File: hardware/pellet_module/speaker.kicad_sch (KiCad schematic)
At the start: 8 parts, among them U3 TPA2005D1

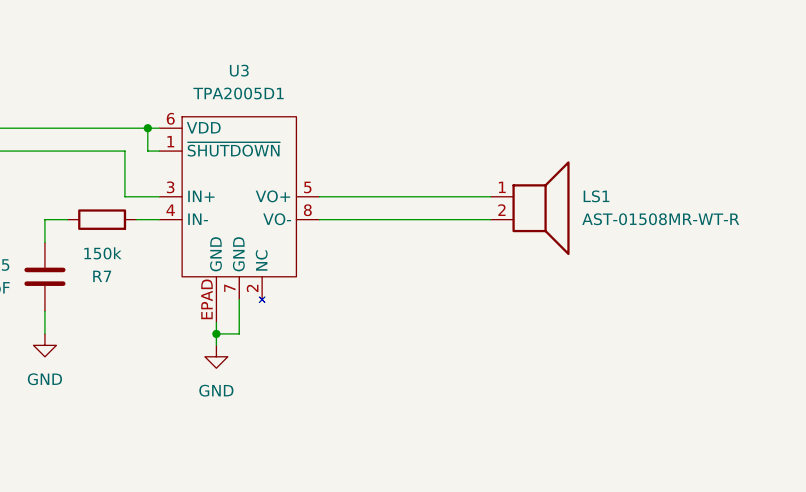
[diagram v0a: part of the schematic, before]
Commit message: add test points, mpns, datasheets
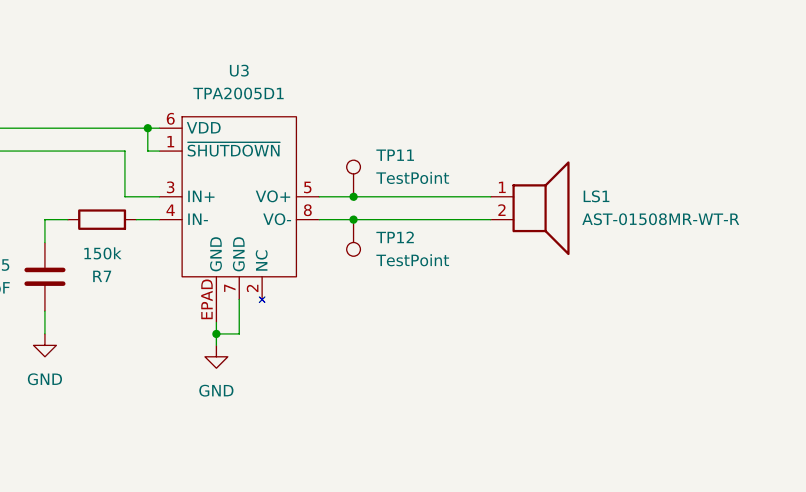
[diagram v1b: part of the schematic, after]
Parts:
- added TP11, TP12: TestPoint, symbol Connector:TestPoint
- C13: footprint (none) -> Capacitor_SMD:C_0603_1608Metric; MPN (none) -> CC0603KRX7R7BB105
- C14, C15: footprint (none) -> Capacitor_SMD:C_0603_1608Metric; MPN (none) -> GRM1885C1H510JA01D
- LS1: MPN (none) -> AST-01508MR-WT-R
- R6: MPN (none) -> RC0603FR-0715KL
- R7: MPN (none) -> RC0603FR-07150KL
- U3: footprint (none) -> Package_SO:HVSSOP-8-1EP_3x3mm_P0.65mm_EP1.57x1.89mm; MPN (none) -> TPA2005D1DRBR
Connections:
- net at LS1.1, U3.5 (VO+): now also TP11.1
- net at LS1.2, U3.8 (VO-): now also TP12.1
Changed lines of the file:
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@@
 	(paper "A4")
+	(junction
+		(at 222.25 96.52)
+		(diameter 0)
+		(color 0 0 0 0)
+	)
 	(junction
 		(at 207.01 111.76)
@@
 		(color 0 0 0 0)
 	)
+	(junction
+		(at 222.25 99.06)
+		(diameter 0)
+		(color 0 0 0 0)
+	)
 	(no_connect
 		(at 173.99 96.52)
@@
 	(wire
 		(pts
+			(xy 222.25 96.52) (xy 237.49 96.52)
+		)
+		(stroke
+			(width 0)
+			(type default)
+		)
+	)
+	(wire
+		(pts
 			(xy 209.55 107.95) (xy 209.55 111.76)
 		)
@@
 	(wire
 		(pts
-			(xy 218.44 96.52) (xy 237.49 96.52)
+			(xy 218.44 96.52) (xy 222.25 96.52)
 		)
 		(stroke
@@
 	(wire
 		(pts
+			(xy 222.25 99.06) (xy 237.49 99.06)
+		)
+		(stroke
+			(width 0)
+			(type default)
+		)
+	)
+	(wire
+		(pts
 			(xy 207.01 110.49) (xy 207.01 111.76)
 		)
@@
 	(wire
 		(pts
-			(xy 218.44 99.06) (xy 237.49 99.06)
+			(xy 218.44 99.06) (xy 222.25 99.06)
 		)
 		(stroke
@@
 			)
 		)
-		(property "MPN" ""
+		(property "MPN" "RC0603FR-0715KL"
 			(at 160.02 96.52 0)
 			(effects
@@
 			)
 		)
-		(property "MPN" ""
+		(property "MPN" "AST-01508MR-WT-R"
 			(at 242.57 96.52 0)
 			(effects
@@
 			)
 		)
-		(property "MPN" ""
+		(property "MPN" "RC0603FR-07150KL"
 			(at 194.31 99.06 0)
 			(effects
@@
 				(path "/48650363-a452-429d-997e-1ddabb69aad0/b6dbd572-5e20-467e-a878-ec4193e43632"
 					(reference "R7")
+					(unit 1)
+				)
+			)
+		)
+	)
+	(symbol
+		(lib_id "Connector:TestPoint")
+		(at 222.25 96.52 0)
+		(unit 1)
+		(exclude_from_sim no)
+		(in_bom yes)
+		(on_board yes)
+		(dnp no)
+		(fields_autoplaced yes)
+		(property "Reference" "TP11"
+			(at 224.79 91.9479 0)
+			(effects
+				(font
+					(size 1.27 1.27)
+				)
+				(justify left)
+			)
+		)
+		(property "Value" "TestPoint"
+			(at 224.79 94.4879 0)
+			(effects
+				(font
+					(size 1.27 1.27)
+				)
+				(justify left)
+			)
+		)
+		(property "Footprint" ""
+			(at 227.33 96.52 0)
+			(effects
+				(font
+					(size 1.27 1.27)
+				)
+				(hide yes)
+			)
+		)
+		(property "Datasheet" "~"
+			(at 227.33 96.52 0)
+			(effects
+				(font
+					(size 1.27 1.27)
+				)
+				(hide yes)
+			)
+		)
+		(property "Description" "test point"
+			(at 222.25 96.52 0)
+			(effects
+				(font
+					(size 1.27 1.27)
+				)
+				(hide yes)
+			)
+		)
+		(pin "1"
+		)
+		(instances
+			(project ""
+				(path "/48650363-a452-429d-997e-1ddabb69aad0/b6dbd572-5e20-467e-a878-ec4193e43632"
+					(reference "TP11")
+					(unit 1)
+				)
+			)
+		)
+	)
+	(symbol
+		(lib_id "Connector:TestPoint")
+		(at 222.25 99.06 180)
+		(unit 1)
+		(exclude_from_sim no)
+		(in_bom yes)
+		(on_board yes)
+		(dnp no)
+		(fields_autoplaced yes)
+		(property "Reference" "TP12"
+			(at 224.79 101.0919 0)
+			(effects
+				(font
+					(size 1.27 1.27)
+				)
+				(justify right)
+			)
+		)
+		(property "Value" "TestPoint"
+			(at 224.79 103.6319 0)
+			(effects
+				(font
+					(size 1.27 1.27)
+				)
+				(justify right)
+			)
+		)
+		(property "Footprint" ""
+			(at 217.17 99.06 0)
+			(effects
+				(font
+					(size 1.27 1.27)
+				)
+				(hide yes)
+			)
+		)
+		(property "Datasheet" "~"
+			(at 217.17 99.06 0)
+			(effects
+				(font
+					(size 1.27 1.27)
+				)
+				(hide yes)
+			)
+		)
+		(property "Description" "test point"
+			(at 222.25 99.06 0)
+			(effects
+				(font
+					(size 1.27 1.27)
+				)
+				(hide yes)
+			)
+		)
+		(pin "1"
+		)
+		(instances
+			(project "pellet"
+				(path "/48650363-a452-429d-997e-1ddabb69aad0/b6dbd572-5e20-467e-a878-ec4193e43632"
+					(reference "TP12")
 					(unit 1)
 				)
@@
 			)
 		)
-		(property "Footprint" ""
+		(property "Footprint" "Package_SO:HVSSOP-8-1EP_3x3mm_P0.65mm_EP1.57x1.89mm"
 			(at 209.55 85.09 0)
 			(effects
@@
 			)
 		)
-		(property "Datasheet" ""
+		(property "Datasheet" "https://www.ti.com/lit/ds/symlink/tpa2005d1.pdf"
 			(at 209.55 85.09 0)
 			(effects
@@
 			)
 		)
-		(property "MPN" ""
+		(property "MPN" "TPA2005D1DRBR"
 			(at 209.55 85.09 0)
 			(effects
@@
 			)
 		)
-		(property "Footprint" ""
+		(property "Footprint" "Capacitor_SMD:C_0603_1608Metric"
 			(at 188.9252 109.22 0)
 			(effects
@@
 			)
 		)
-		(property "MPN" ""
+		(property "MPN" "GRM1885C1H510JA01D"
 			(at 187.96 105.41 0)
 			(effects
@@
 			)
 		)
-		(property "Footprint" ""
+		(property "Footprint" "Capacitor_SMD:C_0603_1608Metric"
 			(at 120.3452 102.87 0)
 			(effects
@@
 			)
 		)
-		(property "MPN" ""
+		(property "MPN" "CC0603KRX7R7BB105"
 			(at 119.38 99.06 0)
 			(effects
@@
 			)
 		)
-		(property "Footprint" ""
+		(property "Footprint" "Capacitor_SMD:C_0603_1608Metric"
 			(at 151.13 97.4852 0)
 			(effects
@@
 			)
 		)
-		(property "MPN" ""
+		(property "MPN" "GRM1885C1H510JA01D"
 			(at 147.32 96.52 0)
 			(effects

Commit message: add titles, ESD protection, make changes requested by Ryan
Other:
- company: (none) -> Christie Lab, CU-Anschutz
- title: (none) -> Autotrainer Pellet Module - Speaker
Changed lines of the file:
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@@
 	(generator_version "8.0")
 	(paper "A4")
+	(title_block
+		(title "Autotrainer Pellet Module - Speaker")
+		(date "2024-07-09")
+		(rev "v1.0")
+		(company "Christie Lab, CU-Anschutz")
+		(comment 1 "Prepared by LeafLabs, LLC")
+	)
 	(junction
 		(at 222.25 96.52)

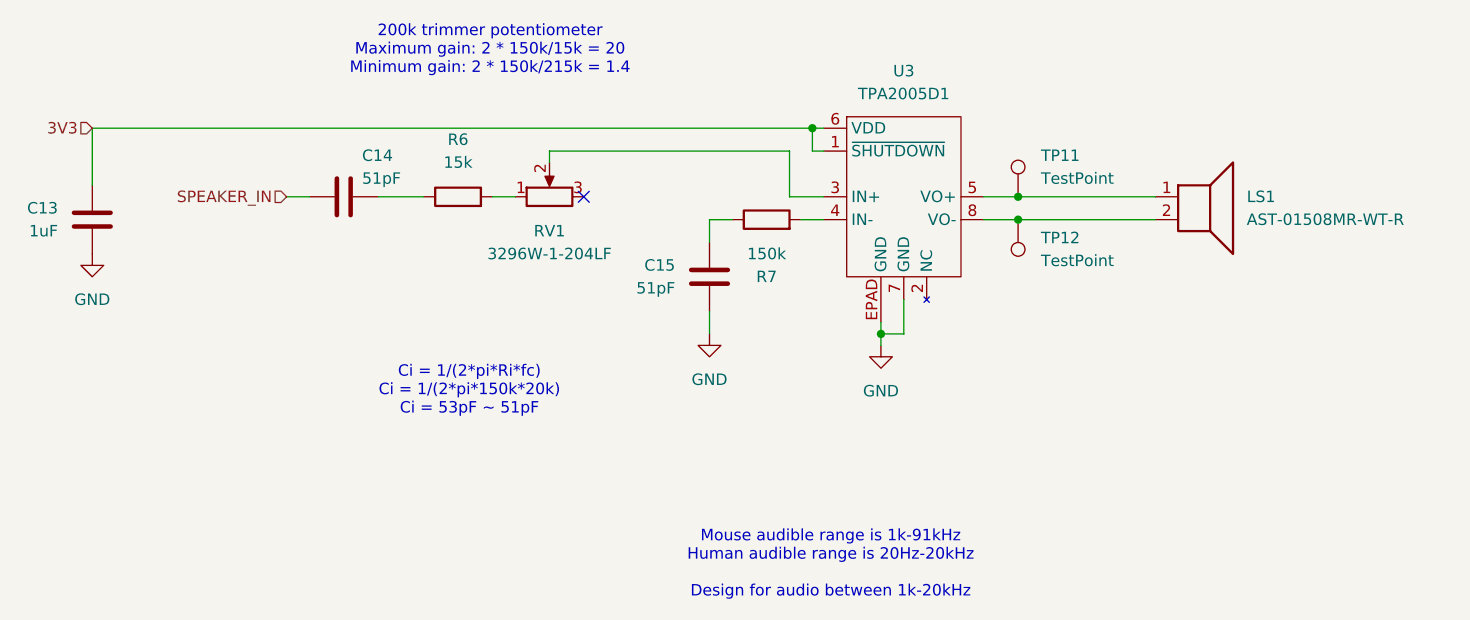
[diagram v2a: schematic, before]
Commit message: * Add footprints for every part * Change power LED from 20mA to 4mA * Edit symbols to match footprints (EPAD -> pin numbers) to eliminate errors on import to pcbnew
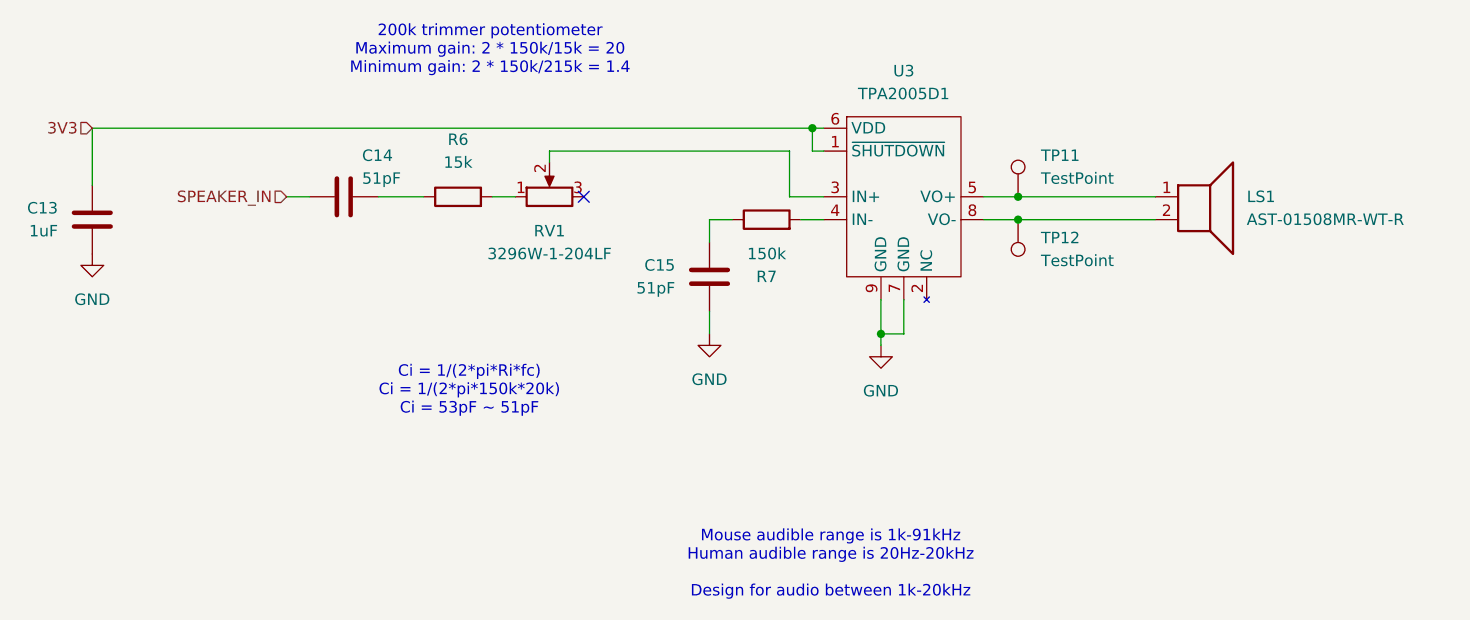
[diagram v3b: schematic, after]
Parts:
- LS1: footprint (none) -> Leaf_Microphone:Speaker_P7.6mm
- R6, R7: footprint (none) -> Resistor_SMD:R_0603_1608Metric
- RV1: footprint (none) -> Potentiometer_THT:Potentiometer_Bourns_3296W_Vertical
- TP11, TP12: footprint (none) -> TestPoint:TestPoint_Pad_1.0x1.0mm
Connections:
- net GND: now also U3.9 (GND); no longer U3.EPAD (GND)
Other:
- moved on the sheet: U3
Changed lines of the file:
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@@
 	(wire
 		(pts
-			(xy 207.01 110.49) (xy 207.01 111.76)
+			(xy 207.01 107.95) (xy 207.01 111.76)
 		)
 		(stroke
@@
 			)
 		)
-		(property "Footprint" ""
+		(property "Footprint" "Resistor_SMD:R_0603_1608Metric"
 			(at 160.02 98.298 90)
 			(effects
@@
 			)
 		)
-		(property "Footprint" ""
+		(property "Footprint" "Potentiometer_THT:Potentiometer_Bourns_3296W_Vertical"
 			(at 170.18 96.52 0)
 			(effects
@@
 			)
 		)
-		(property "Footprint" ""
+		(property "Footprint" "Leaf_Microphone:Speaker_P7.6mm"
 			(at 242.57 101.6 0)
 			(effects
@@
 			)
 		)
-		(property "Footprint" ""
+		(property "Footprint" "Resistor_SMD:R_0603_1608Metric"
 			(at 194.31 100.838 90)
 			(effects
@@
 			)
 		)
-		(property "Footprint" ""
+		(property "Footprint" "TestPoint:TestPoint_Pad_1.0x1.0mm"
 			(at 227.33 96.52 0)
 			(effects
@@
 			)
 		)
-		(property "Footprint" ""
+		(property "Footprint" "TestPoint:TestPoint_Pad_1.0x1.0mm"
 			(at 217.17 99.06 0)
 			(effects
@@
 		(pin "5"
 		)
-		(pin "EPAD"
+		(pin "9"
 		)
 		(pin "3"

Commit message: Releases layout for pellet, magnet, and Jetson breakout boards.
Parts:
- C13: LCSC (none) -> C15849; MPN CC0603KRX7R7BB105 -> CL10A105KB8NNNC
- C14, C15: LCSC (none) -> C162235
- LS1: LCSC (none) -> C3311279
- R6: LCSC (none) -> C22809; MPN RC0603FR-0715KL -> 0603WAF1502T5E
- R7: LCSC (none) -> C22807; MPN RC0603FR-07150KL -> 0603WAF1503T5E
- RV1: LCSC (none) -> C58354
- TP11, TP12: now left out of the parts list
- U3: footprint Package_SO:HVSSOP-8-1EP_3x3mm_P0.65mm_EP1.57x1.89mm -> Leaf_InterfaceIC:HVSSOP-8-1EP_3x3mm_P0.65mm_EP1.57x1.89mm_SmallPads; LCSC (none) -> C27396; MPN TPA2005D1DRBR -> TPA2005D1DGNR
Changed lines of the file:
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@@
 			)
 		)
-		(property "MPN" "RC0603FR-0715KL"
+		(property "MPN" "0603WAF1502T5E"
+			(at 160.02 96.52 0)
+			(effects
+				(font
+					(size 1.27 1.27)
+				)
+				(hide yes)
+			)
+		)
+		(property "LCSC" "C22809"
 			(at 160.02 96.52 0)
 			(effects
@@
 			)
 		)
+		(property "LCSC" "C58354"
+			(at 170.18 96.52 0)
+			(effects
+				(font
+					(size 1.27 1.27)
+				)
+				(hide yes)
+			)
+		)
 		(pin "3"
 		)
@@
 			)
 		)
+		(property "LCSC" "C3311279"
+			(at 242.57 96.52 0)
+			(effects
+				(font
+					(size 1.27 1.27)
+				)
+				(hide yes)
+			)
+		)
 		(pin "2"
 		)
@@
 			)
 		)
-		(property "MPN" "RC0603FR-07150KL"
+		(property "MPN" "0603WAF1503T5E"
+			(at 194.31 99.06 0)
+			(effects
+				(font
+					(size 1.27 1.27)
+				)
+				(hide yes)
+			)
+		)
+		(property "LCSC" "C22807"
 			(at 194.31 99.06 0)
 			(effects
@@
 		(unit 1)
 		(exclude_from_sim no)
-		(in_bom yes)
+		(in_bom no)
 		(on_board yes)
 		(dnp no)
@@
 		(unit 1)
 		(exclude_from_sim no)
-		(in_bom yes)
+		(in_bom no)
 		(on_board yes)
 		(dnp no)
@@
 			)
 		)
-		(property "Footprint" "Package_SO:HVSSOP-8-1EP_3x3mm_P0.65mm_EP1.57x1.89mm"
+		(property "Footprint" "Leaf_InterfaceIC:HVSSOP-8-1EP_3x3mm_P0.65mm_EP1.57x1.89mm_SmallPads"
 			(at 209.55 85.09 0)
 			(effects
@@
 			)
 		)
-		(property "MPN" "TPA2005D1DRBR"
+		(property "MPN" "TPA2005D1DGNR"
+			(at 209.55 85.09 0)
+			(effects
+				(font
+					(size 1.27 1.27)
+				)
+				(hide yes)
+			)
+		)
+		(property "LCSC" "C27396"
 			(at 209.55 85.09 0)
 			(effects
@@
 			)
 		)
+		(property "LCSC" "C162235"
+			(at 187.96 105.41 0)
+			(effects
+				(font
+					(size 1.27 1.27)
+				)
+				(hide yes)
+			)
+		)
 		(pin "1"
 		)
@@
 			)
 		)
-		(property "MPN" "CC0603KRX7R7BB105"
+		(property "MPN" "CL10A105KB8NNNC"
+			(at 119.38 99.06 0)
+			(effects
+				(font
+					(size 1.27 1.27)
+				)
+				(hide yes)
+			)
+		)
+		(property "LCSC" "C15849"
 			(at 119.38 99.06 0)
 			(effects
@@
 			(at 147.32 96.52 0)
 			(effects
+				(font
+					(size 1.27 1.27)
+				)
+				(hide yes)
+			)
+		)
+		(property "LCSC" "C162235"
+			(at 147.32 96.52 0)
+			(effects
